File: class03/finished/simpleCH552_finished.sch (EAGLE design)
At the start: 12 parts, among them U1 CH552G, X1 USBPCB

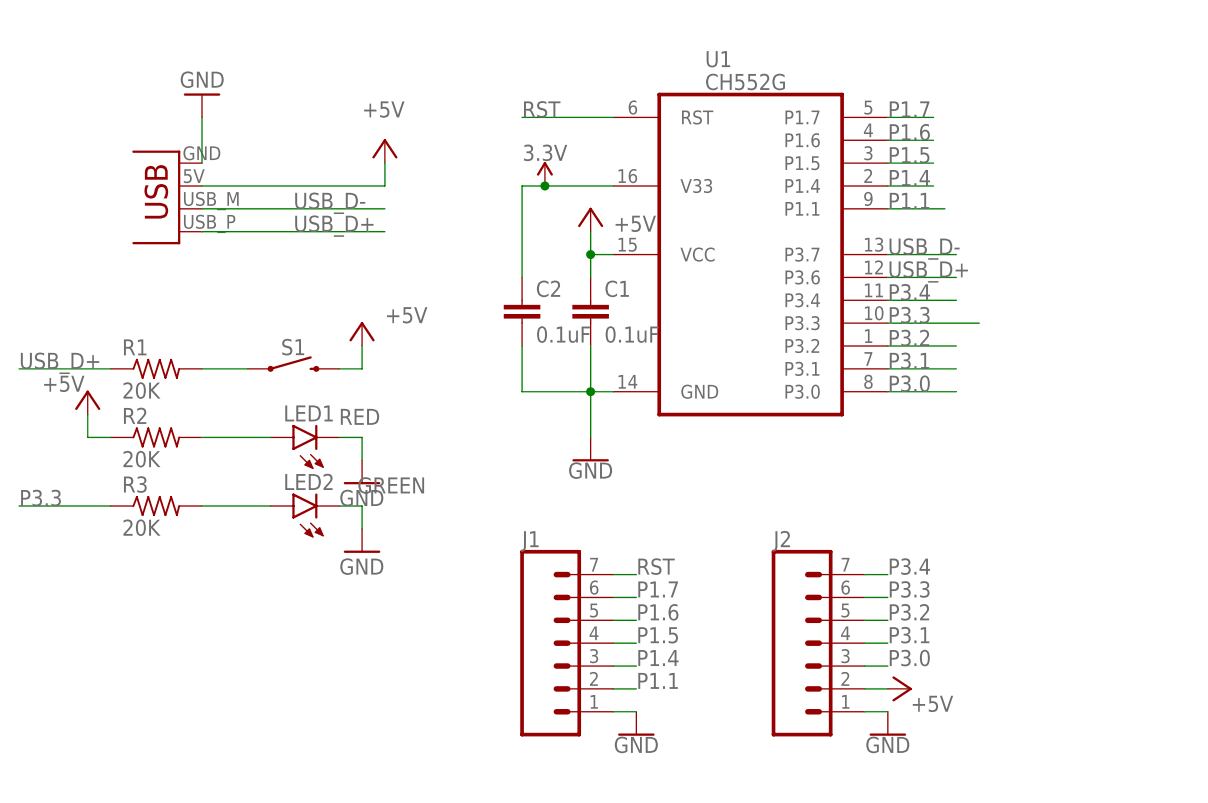
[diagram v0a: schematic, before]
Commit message: update to USB shell model
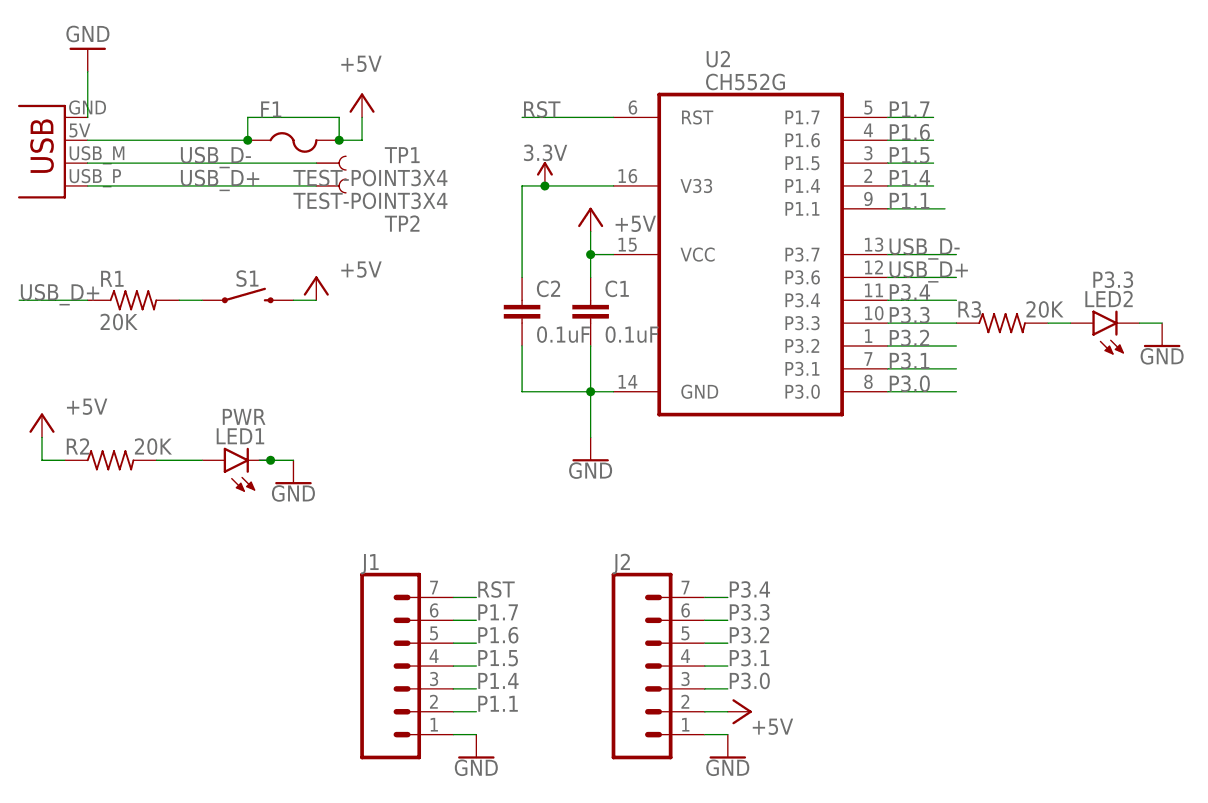
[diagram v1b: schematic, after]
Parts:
- added F1: (no value), adafruit:PTCFUSE-1206
- added TP1, TP2: TEST-POINT3X4, SparkFun-Connectors:TEST-POINT3X4
- LED1: value RED -> PWR; device led:LEDCHIP-LED0805 -> BeagleBone_Black_Wireless:GHI-BASICCOMPONENTS_LED-(INCH)-0805
- LED2: value GREEN -> P3.3; device led:LEDCHIP-LED0805 -> BeagleBone_Black_Wireless:GHI-BASICCOMPONENTS_LED-(INCH)-0805
- renumbered U1 to U2
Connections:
- net +5V: now also F1.1, F1.2
- net GND: now also LED1.K, LED2.K; no longer LED1.C, LED2.C
- net USB_D+: now also TP2.1
- net USB_D-: now also TP1.1
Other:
- moved on the sheet: J1, J2, R1, R2, R3, S1
